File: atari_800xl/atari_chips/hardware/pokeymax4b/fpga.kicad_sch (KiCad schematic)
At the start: 11 parts, among them J2 Conn_02x03_Odd_Even, Y1 ASE-49.152MHz

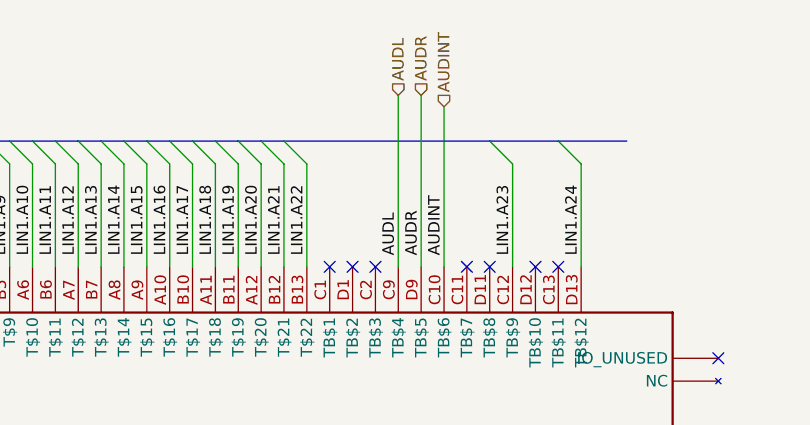
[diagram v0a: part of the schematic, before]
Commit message: After testing 4b first run, there are a few issues. Updated to 4b2 with: Corrected L/R output. ADC bias improvement. ADC preamp out/in- corrected. Moved silkscreen name!
git-svn-id: svn+ssh://192.168.0.3/home/svnfpga/repo/trunk@1475 d6161ac3-aae1-4d52-9b05-ea9ac36b53d3
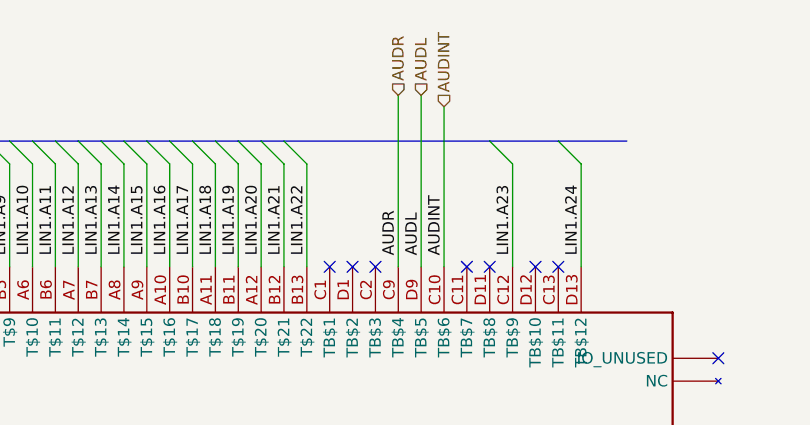
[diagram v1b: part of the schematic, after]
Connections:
- net AUDL: now also U3.D9 (TB$5); no longer U3.C9 (TB$4)
- net AUDR: now also U3.C9 (TB$4); no longer U3.D9 (TB$5)
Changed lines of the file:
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@@
 		)
 	)
-	(label "AUDR"
+	(label "AUDL"
 		(at 154.94 36.83 90)
 		(effects
@@
 		)
 	)
-	(label "AUDL"
+	(label "AUDR"
 		(at 152.4 36.83 90)
 		(effects
@@
 		)
 	)
-	(hierarchical_label "AUDL"
+	(hierarchical_label "AUDR"
 		(shape input)
 		(at 152.4 19.05 90)
@@
 		)
 	)
-	(hierarchical_label "AUDR"
+	(hierarchical_label "AUDL"
 		(shape input)
 		(at 154.94 19.05 90)
